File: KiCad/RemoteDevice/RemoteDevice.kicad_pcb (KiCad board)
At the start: 2 copper layers, 93 x 52.5 mm, 42 parts, among them J1 Alim, J2 CN1, Q1 Si4435, SW1 BP, SW2 BP, U1 XC9140, U2 STM32L041F6Px, U3 MCP6281, U4 ADT7410TRZ, U5 MCP6281, U6 RT606, U7 Microphone

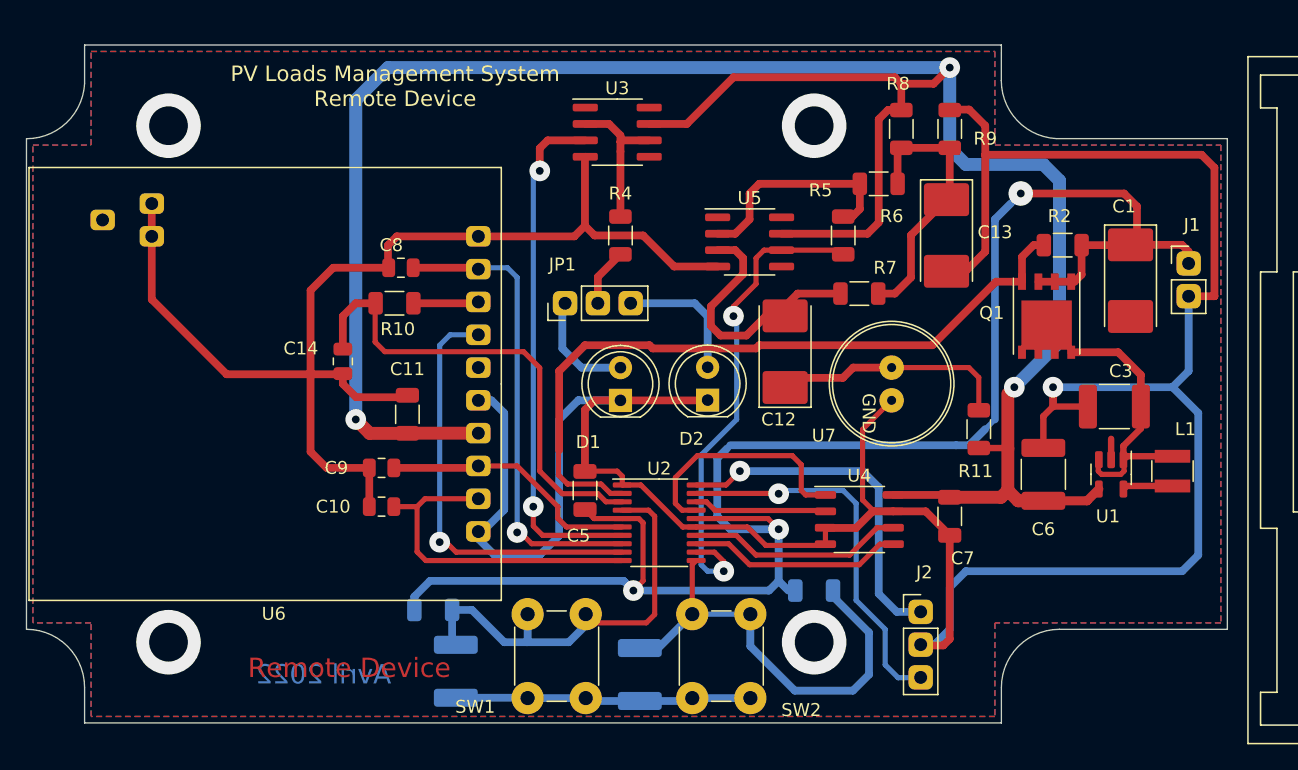
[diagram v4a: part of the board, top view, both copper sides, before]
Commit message: Revue des plans de masses pour qu'ils prennent une forme arrondie automatiquement avec edge cut, remap check IO OK, vérifié avec CubeMx 32L041F6
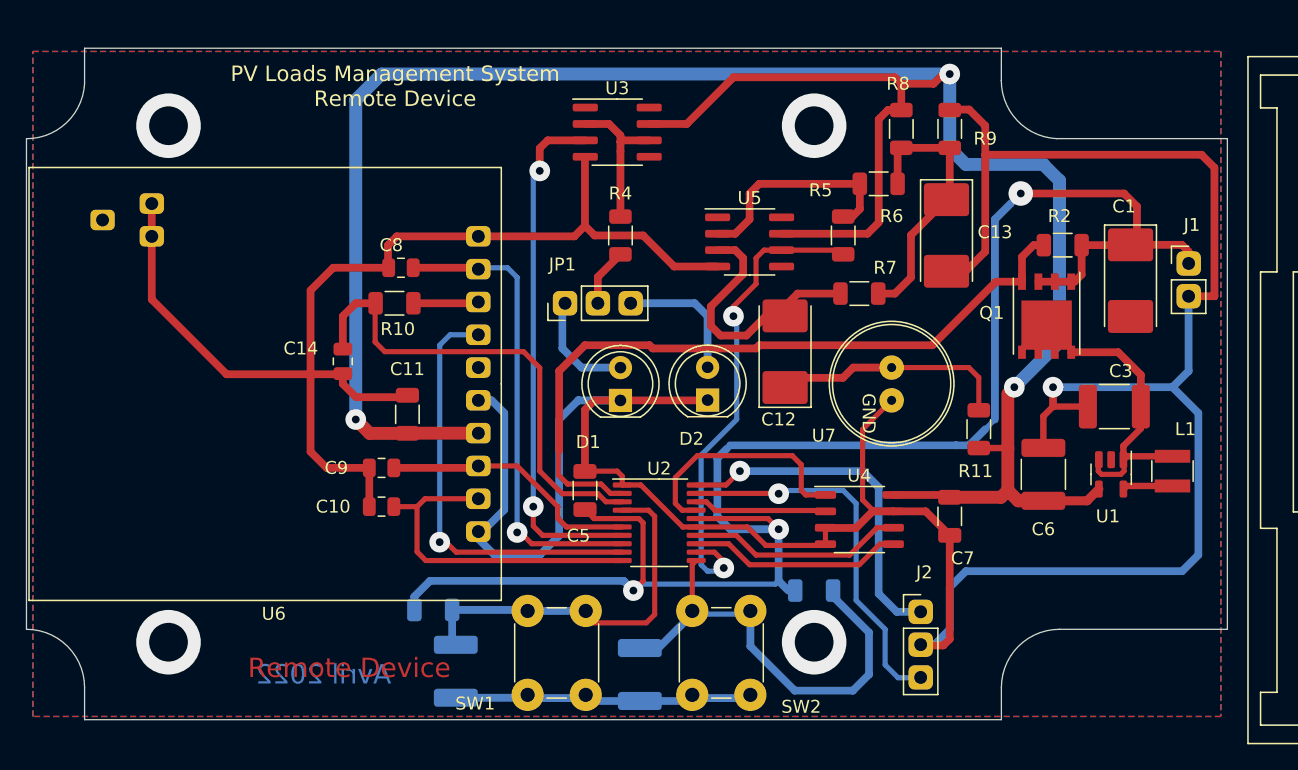
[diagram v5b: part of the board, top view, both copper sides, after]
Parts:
- moved SW1 0.25 mm to (69.0, 109.8)
- moved SW2 0.25 mm to (81.8, 109.8)
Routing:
- net /Reset: track 34.0 -> 29.4 mm
- net GND: track 332.6 -> 330.7 mm
- net +5V: track 187.9 -> 187.0 mm
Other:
- board size 93 x 52.5 mm -> 93 x 52 mm

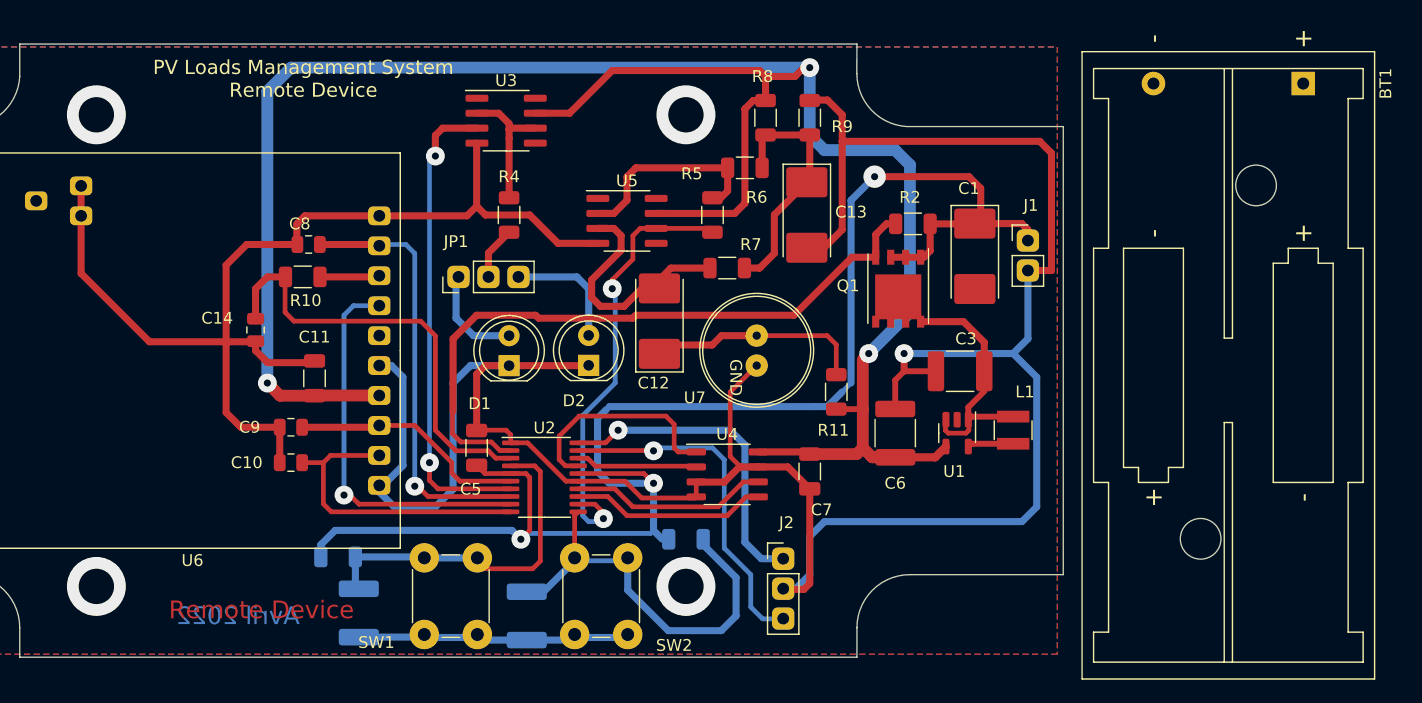
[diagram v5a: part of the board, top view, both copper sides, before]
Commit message: Version béta, production josé GEI, ajout d'une résistance série sur le micro pour ne pas griller l'IO (5V max)
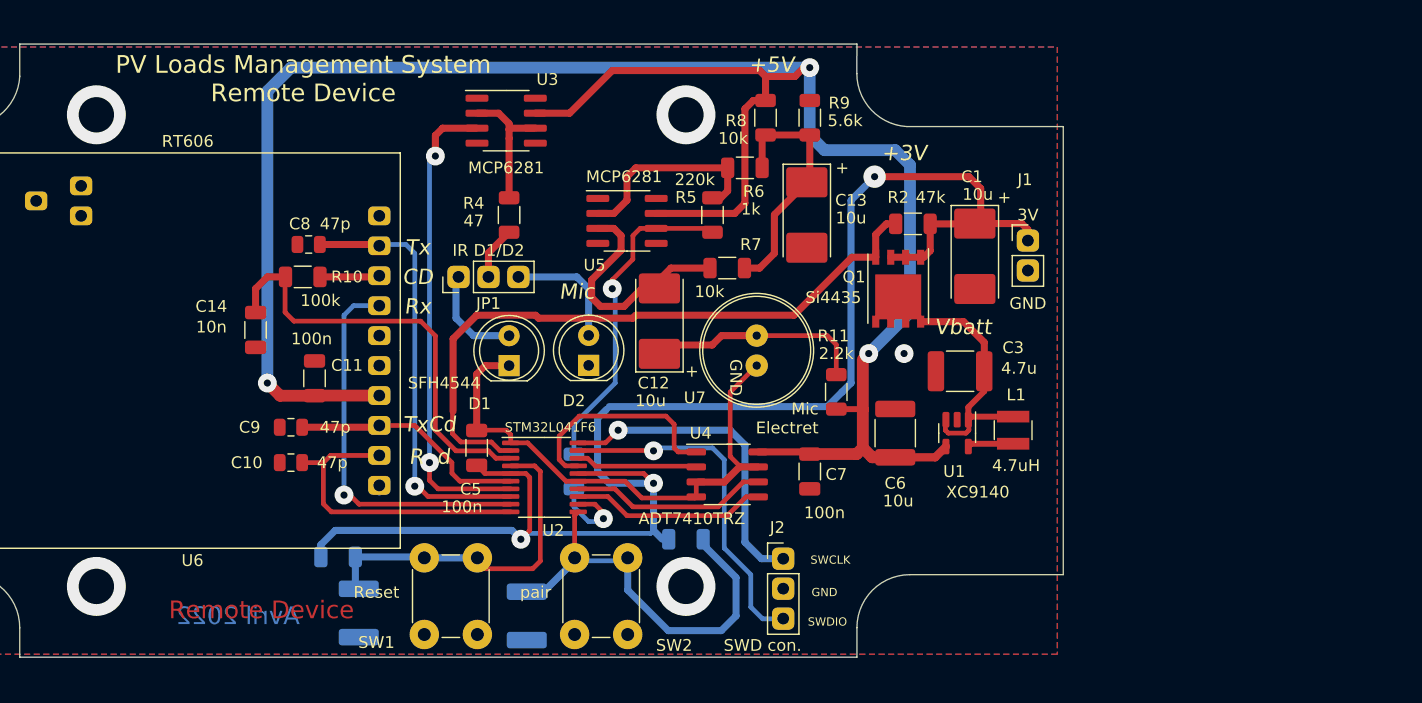
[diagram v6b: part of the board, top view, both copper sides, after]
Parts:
- removed BT1: Battery 3V, Battery:BatteryHolder_Keystone_2468_2xAAA
- added R12: 4.7k, Resistor_SMD:R_1206_3216Metric, B.Cu at (79.5, 99.2)
- C14: value 47p -> 10n; footprint Capacitor_SMD:C_0805_2012Metric -> Capacitor_SMD:C_1206_3216Metric
- R10: value R -> 100k
- R11: value R -> 2.2k
- R2: value R -> 47k
- R3: value R -> 4.7k
- R4: value R -> 47
- R5: value R -> 220k
- R6: value R -> 1k
- R7, R8: value R -> 10k
- R9: value R -> 5.6k
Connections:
- R5 pad 2: /MicroPhone -> Net-(R5-Pad2)
- U5 pad 6: /MicroPhone -> Net-(R5-Pad2)
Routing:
- net GND: track 330.7 -> 47.5 mm
- net /MicroPhone: track 38.8 -> 7.74 mm, vias 2 -> 1
- net Net-(R5-Pad2): track 0.00 -> 28.7 mm, vias 0 -> 1
- net /CarrierDetect: track 37.5 -> 36.9 mm
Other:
- board text added: "+"
- board text added: "+3V"
- board text added: "+5V"
- board text added: "100k"
- board text added: "100n"
- board text added: "10k"
- board text added: "10n"
- board text added: "10u"
- board text added: "1k"
- board text added: "2.2k"
- board text added: "2.2u"
- board text added: "220k"
- board text added: "3V"
- board text added: "4.7k"
- board text added: "4.7u"
- board text added: "4.7uH"
- board text added: "47"
- board text added: "47k"
- board text added: "47p"
- board text added: "5.6k"
- board text added: "ADT7410TRZ"
- board text added: "CD"
- board text added: "GND"
- board text added: "IR D1/D2"
- board text added: "MCP6281"
- board text added: "Mic"
- board text added: "Mic Electret"
- board text added: "R d"
- board text added: "RT606"
- board text added: "Reset"
- board text added: "Rx"
- board text added: "SFH4544"
- board text added: "STM32L041F6"
- board text added: "SWCLK"
- board text added: "SWD con."
- board text added: "SWDIO"
- board text added: "Si4435"
- board text added: "Tx"
- board text added: "TxCd"
- board text added: "Vbatt"
- board text added: "XC9140"
- board text added: "pair"
